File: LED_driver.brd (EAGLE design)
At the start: 100 x 80 mm, 15 parts

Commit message: Almost done with version 1 of the LED Driver Board
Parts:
- removed C4: 4.7uF 80V, resistor:C1210
- removed C6: 10uF, resistor:C0603
- removed U$11: VREG-ZXTR2105, BlueRobotics-Main:SOT23-3
- removed U$3: 10uH, BlueRobotics-Main:INDUCTOR-8040
- added C8: 47uF, PowerComponents:CTAN(7.30_4.30MM)
- added J1: (no value), SparkFun-Connectors:1X01
- added J8, J9: (no value), SparkFun-Connectors:1X02_NO_SILK
- added U$4: 15uH, DiscreteComponents:HCMA1305
- C3: value 47uF 63V -> 4.7uF; device SparkFun-Capacitors:CPOL-RADIAL-100UF-25V -> rcl:C0603
- moved U$2 17.2 mm to (24.1, 45.0)
- moved R7 13.2 mm to (11.9, 13.2), turned to 180 degrees
- moved C7 12.9 mm to (7.37, 13.2), turned to 180 degrees
- moved C5 9.32 mm to (7.37, 15.5), turned to 180 degrees
- moved D1 7.64 mm to (2.79, 13.2), flipped to the bottom
- moved U$1 6.36 mm to (9.91, 12.7)
- moved C1 6.10 mm to (11.2, 15.7)
- moved R1 5.00 mm to (16.3, 7.62)
- moved R2 4.38 mm to (9.14, 8.89)
- moved C2 3.57 mm to (14.2, 19.1), flipped to the bottom, turned to 180 degrees
- moved C3 3.25 mm to (6.60, 9.40), flipped to the bottom, turned to 90 degrees
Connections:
- removed net VCC: C6.1, U$11.2
- net GND: now also C8.-, J8.1, J8.2; no longer C4.2, C6.2, U$11.1
- net LED+: now also U$4.P$2; no longer U$3.P$2
- net LED-PWM: now also J1.1
- net N$5: now also U$4.P$1; no longer U$3.P$1
- net VIN: now also C8.+, J9.1, J9.2; no longer C4.1, U$11.3
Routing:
- net LED-PWM: track 0.00 -> 8.34 mm
- net N$4: track 0.00 -> 4.62 mm, vias 0 -> 1
- net GND: track 0.00 -> 3.94 mm, vias 0 -> 7
- net N$1: track 0.00 -> 3.79 mm, vias 0 -> 1
- net VCC6211: track 0.00 -> 3.48 mm, vias 0 -> 1
- net VIN: track 0.00 -> 3.12 mm, vias 0 -> 1
- net N$2: track 0.00 -> 2.30 mm
- net LED+: track 0.00 -> 1.84 mm, vias 0 -> 1
- net LED-: track 0.00 -> 1.59 mm, vias 0 -> 1
- added copper zone on layer 1, net GND
- added copper zone on layer 16, net GND
- added copper zone on layer 1, net LED+
- added copper zone on layer 1, net LED-
- added copper zone on layer 1, net N$5
- added copper zone on layer 16, net N$5
- added copper zone on layer 1, net VIN
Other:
- board size 100 x 80 mm -> 20.3 x 37.3 mm

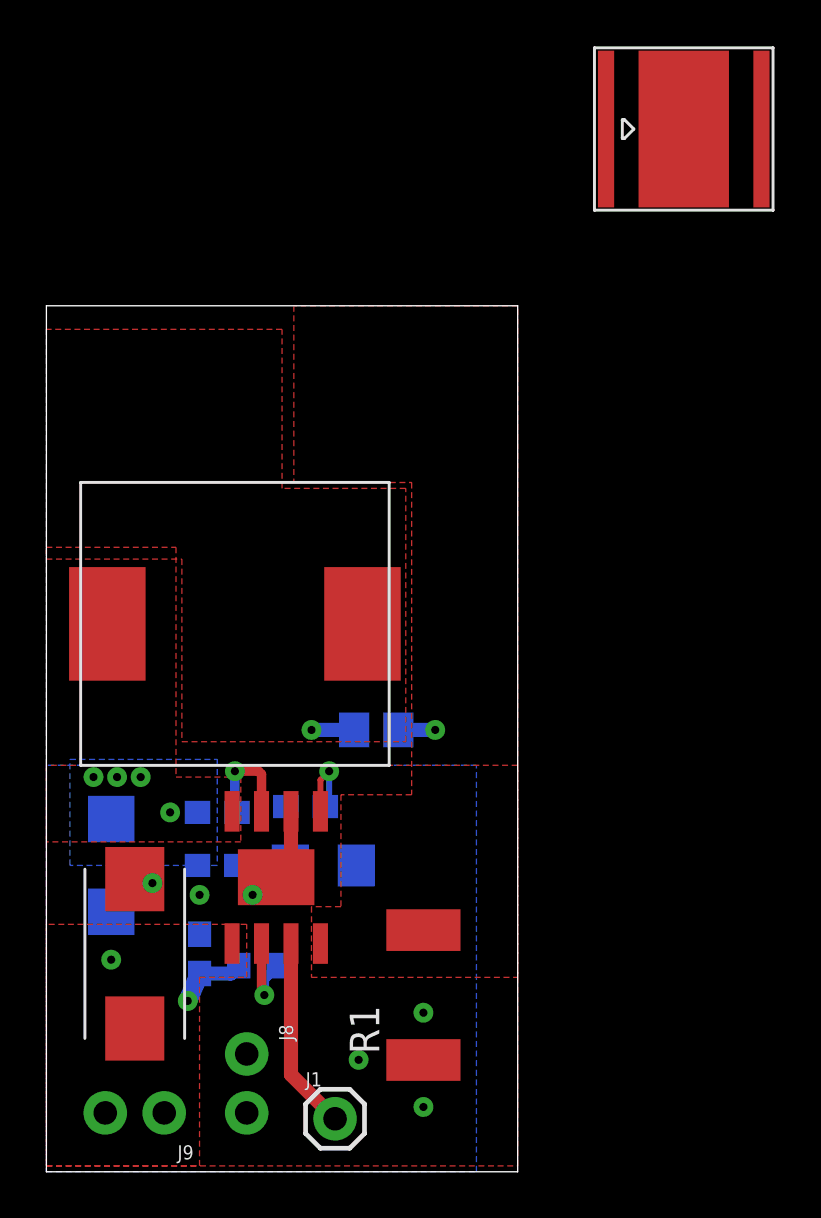
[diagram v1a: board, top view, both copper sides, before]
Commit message: Grant's design with the cheaper LED placed on the board
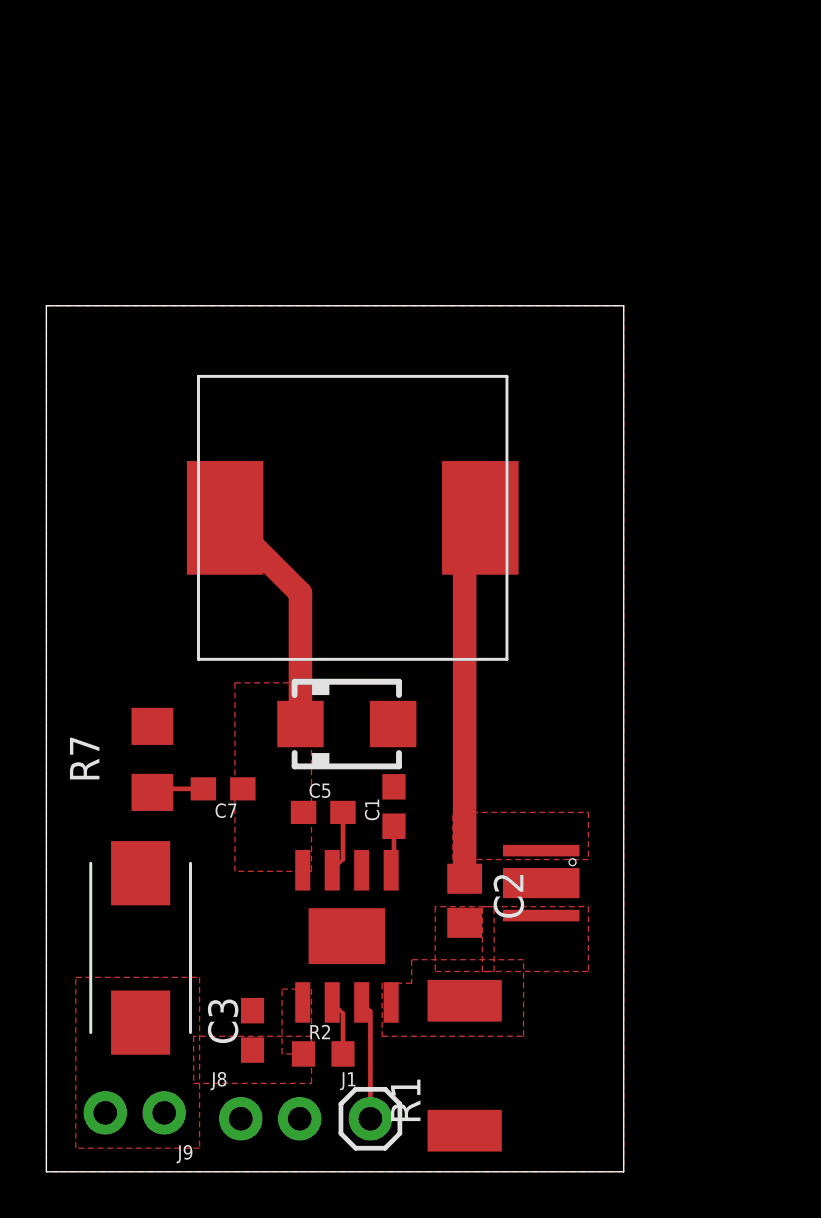
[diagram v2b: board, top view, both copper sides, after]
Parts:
- removed U$2: LED-MK-R, BlueRobotics-Main:MK-R
- added U$3: LED_00H53, LED_00H53:LED_00H53
- moved D1 11.8 mm to (13.0, 19.3), flipped to the top, turned to 0 degrees
- moved R7 8.67 mm to (4.57, 17.8), flipped to the top, turned to 90 degrees
- moved C2 8.29 mm to (18.0, 11.7), flipped to the top, turned to 270 degrees
- moved U$4 6.83 mm to (13.2, 28.2)
- moved R2 4.72 mm to (11.9, 5.08), flipped to the top, turned to 0 degrees
- moved C5 4.57 mm to (11.9, 15.5), flipped to the top, turned to 0 degrees
- moved C3 4.02 mm to (8.89, 6.10), flipped to the top
- moved U$1 3.97 mm to (13.0, 10.2)
- moved C1 3.81 mm to (15.0, 15.7), flipped to the top, turned to 90 degrees
- moved R1 3.53 mm to (18.0, 4.57)
- moved C7 3.31 mm to (7.62, 16.5), flipped to the top
- moved J8 2.81 mm to (8.38, 2.29), turned to 0 degrees
- moved J1 1.52 mm to (14.0, 2.29)
- moved C8 0.36 mm to (4.06, 9.65)
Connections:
- removed net EXT: U$2.EXP
- removed net LED+ISO: U$2.A
- removed net LED-ISO: U$2.C
- net LED+: now also U$3.LED+
- net LED-: now also U$3.LED-
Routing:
- net LED+: track 1.84 -> 15.8 mm, vias 1 -> 0
- net N$5: track 0.00 -> 10.2 mm, vias 4 -> 0
- net GND: track 3.94 -> 0.00 mm, vias 7 -> 0
- net LED-PWM: track 8.34 -> 5.17 mm
- net VIN: track 3.12 -> 0.00 mm, vias 1 -> 0
- net N$4: track 4.62 -> 2.69 mm, vias 1 -> 0
- net LED-: track 1.59 -> 0.00 mm, vias 1 -> 0
- net VCC6211: track 3.48 -> 1.95 mm, vias 1 -> 0
- net N$1: track 3.79 -> 2.41 mm, vias 1 -> 0
- removed copper zone on layer 16, net GND
- removed copper zone on layer 16, net N$5
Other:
- board size 20.3 x 37.3 mm -> 24.9 x 37.3 mm

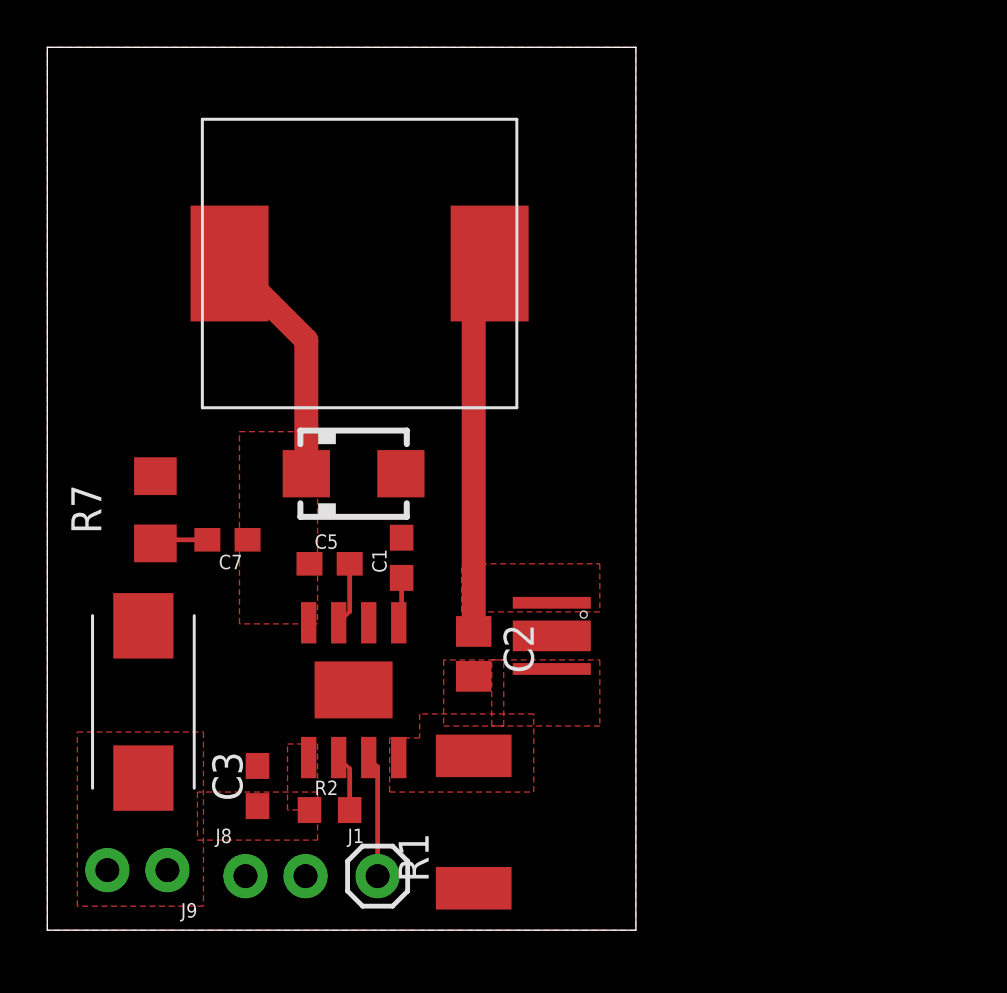
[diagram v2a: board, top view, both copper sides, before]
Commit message: Changed layout so LED is on the end of the board. Fixed traces
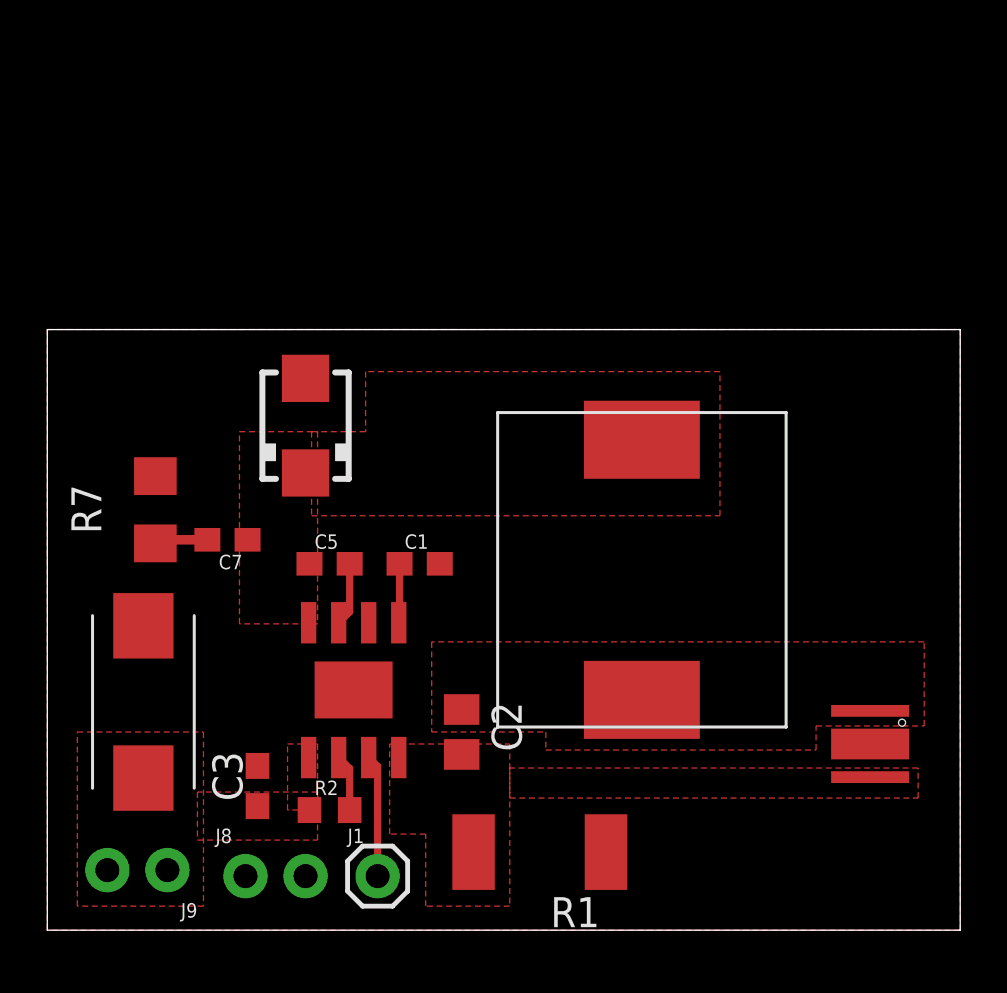
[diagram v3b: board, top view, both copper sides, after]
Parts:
- moved U$4 17.6 mm to (25.1, 15.2), turned to 0 degrees
- moved U$3 14.2 mm to (34.8, 7.87)
- moved C2 3.34 mm to (17.5, 8.38)
- moved R1 3.07 mm to (20.8, 3.30), turned to 180 degrees
- moved D1 2.87 mm to (10.9, 21.3), turned to 90 degrees
- moved C1 0.80 mm to (15.7, 15.5), turned to 0 degrees
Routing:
- net LED+: track 15.8 -> 0.00 mm
- net N$5: track 10.2 -> 0.00 mm
- net VCC6211: track 1.95 -> 2.58 mm
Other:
- board size 24.9 x 37.3 mm -> 38.6 x 25.4 mm
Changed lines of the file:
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@@
 <board>
 <plain>
-<wire x1="0" y1="0" x2="24.892" y2="0" width="0" layer="20"/>
-<wire x1="24.892" y1="0" x2="24.892" y2="37.338" width="0" layer="20"/>
-<wire x1="24.892" y1="37.338" x2="0" y2="37.338" width="0" layer="20"/>
-<wire x1="0" y1="37.338" x2="0" y2="0" width="0" layer="20"/>
+<wire x1="0" y1="0" x2="38.608" y2="0" width="0" layer="20"/>
+<wire x1="38.608" y1="0" x2="38.608" y2="25.4" width="0" layer="20"/>
+<wire x1="38.608" y1="25.4" x2="0" y2="25.4" width="0" layer="20"/>
+<wire x1="0" y1="25.4" x2="0" y2="0" width="0" layer="20"/>
 </plain>
 <attributes>
@@
 </autorouter>
 <elements>
-<element name="C1" library="resistor" package="C0603" value="0.1uF" x="14.986" y="15.748" smashed="yes" rot="R90">
-<attribute name="NAME" x="14.351" y="15.113" size="0.6096" layer="25" rot="R90"/>
-<attribute name="VALUE" x="16.256" y="15.113" size="0.6096" layer="27" rot="R90"/>
-</element>
-<element name="C2" library="resistor" package="C0805" value="0.68uF 100V" x="18.034" y="11.684" smashed="yes" rot="R270">
-<attribute name="NAME" x="19.304" y="12.954" size="1.27" layer="25" rot="R270"/>
+<element name="C1" library="resistor" package="C0603" value="0.1uF" x="15.748" y="15.494" smashed="yes">
+<attribute name="NAME" x="15.113" y="16.129" size="0.6096" layer="25"/>
+<attribute name="VALUE" x="15.113" y="14.224" size="0.6096" layer="27"/>
+</element>
+<element name="C2" library="resistor" package="C0805" value="0.68uF 100V" x="17.526" y="8.382" smashed="yes" rot="R270">
+<attribute name="NAME" x="18.796" y="9.652" size="1.27" layer="25" rot="R270"/>
 </element>
 <element name="C5" library="resistor" package="C0603" value="0.1uF" x="11.938" y="15.494"/>
 <element name="C7" library="resistor" package="C0603" value="NP" x="7.62" y="16.51" rot="R180"/>
-<element name="D1" library="BlueRobotics-Main" package="SMA" value="60V 3A" x="12.954" y="19.304" smashed="yes"/>
-<element name="R1" library="resistor" package="R2512" value="0.082 1W" x="18.034" y="4.572" smashed="yes" rot="R90">
-<attribute name="NAME" x="16.129" y="2.032" size="1.27" layer="25" rot="R90"/>
+<element name="D1" library="BlueRobotics-Main" package="SMA" value="60V 3A" x="10.922" y="21.336" smashed="yes" rot="R90"/>
+<element name="R1" library="resistor" package="R2512" value="0.082 1W" x="20.828" y="3.302" smashed="yes" rot="R180">
+<attribute name="NAME" x="23.368" y="1.397" size="1.27" layer="25" rot="R180"/>
 </element>
 <element name="R2" library="resistor" package="R0603" value="140K" x="11.938" y="5.08"/>
@@
 </element>
 <element name="U$1" library="BlueRobotics-Main" package="SOIC8N-LJ" value="A6211" x="12.954" y="10.16" smashed="yes"/>
-<element name="U$4" library="DiscreteComponents" package="HCMA1305" value="15uH" x="13.208" y="28.194" smashed="yes" rot="R90"/>
+<element name="U$4" library="DiscreteComponents" package="HCMA1305" value="15uH" x="25.146" y="15.24" smashed="yes"/>
 <element name="C8" library="PowerComponents" package="CTAN(7.30_4.30MM)" value="47uF" x="4.064" y="9.652" smashed="yes" rot="R90"/>
 <element name="J1" library="SparkFun-Connectors" library_urn="urn:adsk.eagle:library:513" package="1X01" package3d_urn="urn:adsk.eagle:package:38028/1" value="" x="13.97" y="2.286"/>
@@
 <element name="J8" library="SparkFun-Connectors" library_urn="urn:adsk.eagle:library:513" package="1X02_NO_SILK" package3d_urn="urn:adsk.eagle:package:38051/1" value="" x="8.382" y="2.286"/>
 <element name="J9" library="SparkFun-Connectors" library_urn="urn:adsk.eagle:library:513" package="1X02_NO_SILK" package3d_urn="urn:adsk.eagle:package:38051/1" value="" x="5.08" y="2.54" rot="R180"/>
-<element name="U$3" library="LED_00H53" package="LED_00H53" value="LED_00H53" x="21.336" y="12.446" rot="R270"/>
+<element name="U$3" library="LED_00H53" package="LED_00H53" value="LED_00H53" x="34.798" y="7.874" rot="R270"/>
 </elements>
 <signals>
@@
 <polygon width="0.1524" layer="1" rank="6">
 <vertex x="0" y="0"/>
-<vertex x="0" y="37.338"/>
-<vertex x="24.892" y="37.338"/>
-<vertex x="24.892" y="0"/>
+<vertex x="0" y="25.4"/>
+<vertex x="38.608" y="25.4"/>
+<vertex x="38.608" y="0"/>
 </polygon>
 </signal>
@@
 <contactref element="U$1" pad="2"/>
 <contactref element="R2" pad="2"/>
-<wire x1="12.788" y1="5.08" x2="12.788" y2="6.836" width="0.2032" layer="1"/>
-<wire x1="12.788" y1="6.836" x2="12.324" y2="7.3" width="0.1524" layer="1"/>
+<wire x1="12.788" y1="5.08" x2="12.788" y2="6.836" width="0.3048" layer="1"/>
+<wire x1="12.788" y1="6.836" x2="12.324" y2="7.3" width="0.3048" layer="1"/>
 </signal>
 <signal name="VIN">
@@
 <contactref element="U$1" pad="3"/>
 <contactref element="J1" pad="1"/>
-<wire x1="13.97" y1="2.286" x2="13.97" y2="6.924" width="0.2032" layer="1"/>
-<wire x1="13.97" y1="6.924" x2="13.594" y2="7.3" width="0.1524" layer="1"/>
+<wire x1="13.97" y1="2.286" x2="13.97" y2="6.924" width="0.3048" layer="1"/>
+<wire x1="13.97" y1="6.924" x2="13.594" y2="7.3" width="0.3048" layer="1"/>
 </signal>
 <signal name="N$4">
 <contactref element="U$1" pad="7"/>
 <contactref element="C5" pad="2"/>
-<wire x1="12.788" y1="15.494" x2="12.788" y2="13.464" width="0.2032" layer="1"/>
-<wire x1="12.788" y1="13.464" x2="12.324" y2="13" width="0.1524" layer="1"/>
+<wire x1="12.788" y1="15.494" x2="12.788" y2="13.464" width="0.3048" layer="1"/>
+<wire x1="12.788" y1="13.464" x2="12.324" y2="13" width="0.3048" layer="1"/>
 </signal>
 <signal name="N$5">
@@
 <vertex x="11.43" y="21.082"/>
 </polygon>
-<wire x1="10.954" y1="19.304" x2="10.954" y2="24.948" width="1.016" layer="1"/>
-<wire x1="10.954" y1="24.948" x2="7.708" y2="28.194" width="1.016" layer="1"/>
+<polygon width="0.3048" layer="1">
+<vertex x="11.176" y="17.526"/>
+<vertex x="28.448" y="17.526"/>
+<vertex x="28.448" y="23.622"/>
+<vertex x="13.462" y="23.622"/>
+<vertex x="13.462" y="21.082"/>
+<vertex x="11.176" y="21.082"/>
+</polygon>
 </signal>
 <signal name="LED+">
 <contactref element="C2" pad="1"/>
 <contactref element="U$4" pad="P$2"/>
-<wire x1="18.034" y1="12.634" x2="18.034" y2="27.52" width="1.016" layer="1"/>
-<wire x1="18.034" y1="27.52" x2="18.708" y2="28.194" width="1.016" layer="1"/>
 <contactref element="U$3" pad="LED+"/>
-<polygon width="0.1524" layer="1">
-<vertex x="17.526" y="15.494"/>
-<vertex x="23.368" y="15.494"/>
-<vertex x="23.368" y="13.462"/>
-<vertex x="17.526" y="13.462"/>
-</polygon>
-<wire x1="21.336" y1="13.846" x2="18.034" y2="12.634" width="0" layer="19" extent="1-1"/>
+<polygon width="0.3048" layer="1">
+<vertex x="16.256" y="8.382"/>
+<vertex x="21.082" y="8.382"/>
+<vertex x="21.082" y="7.62"/>
+<vertex x="32.512" y="7.62"/>
+<vertex x="32.512" y="8.636"/>
+<vertex x="37.084" y="8.636"/>
+<vertex x="37.084" y="12.192"/>
+<vertex x="16.256" y="12.192"/>
+</polygon>
 </signal>
 <signal name="LED-">
@@
 <contactref element="R1" pad="2"/>
 <contactref element="U$1" pad="4"/>
-<polygon width="0.1524" layer="1">
-<vertex x="14.478" y="5.842"/>
-<vertex x="20.574" y="5.842"/>
-<vertex x="20.574" y="9.144"/>
-<vertex x="15.748" y="9.144"/>
-<vertex x="15.748" y="8.128"/>
-<vertex x="14.478" y="8.128"/>
-</polygon>
-<polygon width="0.1524" layer="1">
-<vertex x="16.764" y="8.636"/>
-<vertex x="19.304" y="8.636"/>
-<vertex x="19.304" y="11.43"/>
-<vertex x="16.764" y="11.43"/>
-</polygon>
 <contactref element="U$3" pad="LED-"/>
-<polygon width="0.1524" layer="1">
-<vertex x="18.796" y="11.43"/>
-<vertex x="23.368" y="11.43"/>
-<vertex x="23.368" y="8.636"/>
-<vertex x="18.796" y="8.636"/>
+<polygon width="0.3048" layer="1">
+<vertex x="14.478" y="7.874"/>
+<vertex x="19.558" y="7.874"/>
+<vertex x="19.558" y="1.016"/>
+<vertex x="16.002" y="1.016"/>
+<vertex x="16.002" y="4.064"/>
+<vertex x="14.478" y="4.064"/>
+</polygon>
+<polygon width="0.1524" layer="1">
+<vertex x="36.83" y="6.858"/>
+<vertex x="19.558" y="6.858"/>
+<vertex x="19.558" y="5.588"/>
+<vertex x="36.83" y="5.588"/>
 </polygon>
 </signal>
@@
 <contactref element="C1" pad="1"/>
 <contactref element="U$1" pad="5"/>
-<wire x1="14.986" y1="14.898" x2="14.986" y2="13.122" width="0.2032" layer="1"/>
 <wire x1="14.986" y1="13.122" x2="14.864" y2="13" width="0.1524" layer="1"/>
+<wire x1="14.898" y1="15.494" x2="14.898" y2="13.21" width="0.3048" layer="1"/>
+<wire x1="14.898" y1="13.21" x2="14.986" y2="13.122" width="0.3048" layer="1"/>
 </signal>
 <signal name="N$2">
 <contactref element="R7" pad="1"/>
 <contactref element="C7" pad="2"/>
-<wire x1="6.77" y1="16.51" x2="4.724" y2="16.51" width="0.2032" layer="1"/>
+<wire x1="6.77" y1="16.51" x2="4.724" y2="16.51" width="0.4064" layer="1"/>
 <wire x1="4.724" y1="16.51" x2="4.572" y2="16.358" width="0.1524" layer="1"/>
 </signal>
